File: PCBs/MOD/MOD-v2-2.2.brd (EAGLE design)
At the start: 159.8 x 49.3 mm, 44 parts, among them J1 SERVO1, J10 JOY1, J11 JOY2, J12 RPi-Shutdown, J13 AN5, J14 AN6, J15 AN7, J16 AN8, J17 Battery (Main), J2 SERVO2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

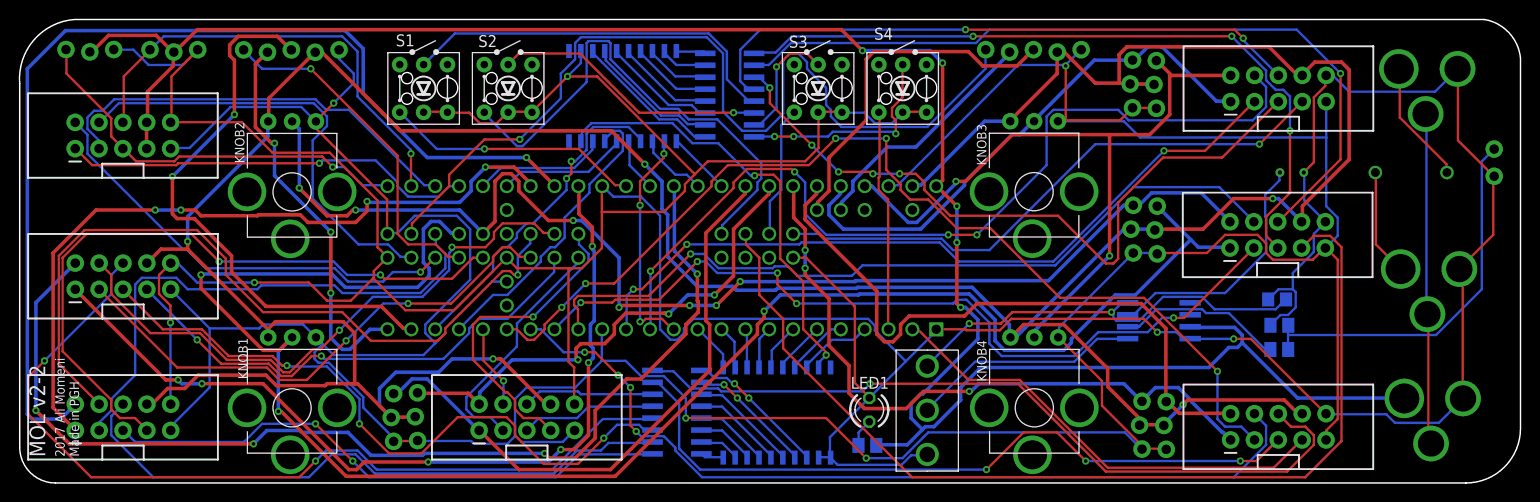
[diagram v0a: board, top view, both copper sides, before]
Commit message: routed teensy breakout for MOD, v2-2.2.brd updated
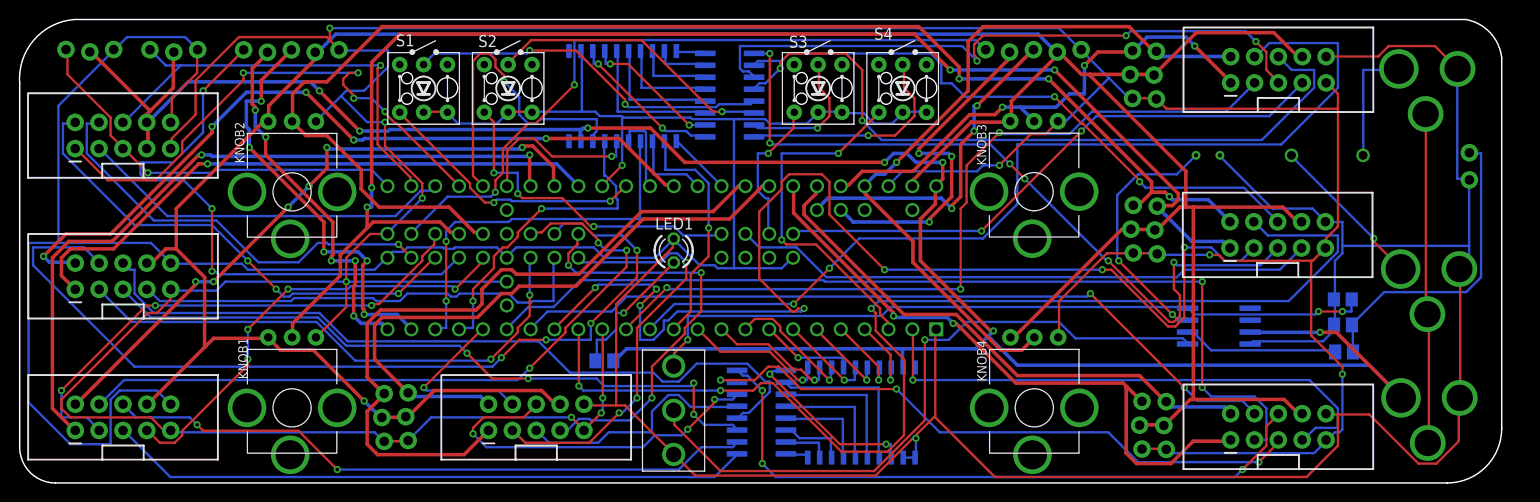
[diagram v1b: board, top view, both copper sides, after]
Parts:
- moved R1 29.4 mm to (62.2, 13.0)
- moved SW2 27.0 mm to (69.6, 7.74)
- moved LED1 26.8 mm to (69.6, 24.7)
- moved RELAY1 9.12 mm to (125.2, 34.9)
- moved RN1 9.00 mm to (79.0, 7.54)
- moved U$1 9.00 mm to (89.6, 7.50)
- moved C1 7.00 mm to (140.9, 19.5)
- moved R2 6.90 mm to (141.0, 13.9)
- moved R3 6.78 mm to (140.9, 16.8)
- moved U1 6.41 mm to (127.7, 16.7)
- moved J12 2.67 mm to (154.3, 35.0)
- moved STRIP6 2.00 mm to (134.0, 44.0)
- moved J13 1.00 mm to (38.7, 4.43)
- moved J14 1.00 mm to (41.2, 4.52)
- moved J8 1.00 mm to (118.3, 40.9)
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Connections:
- removed net V+: U$1.9, U$2.9
- net +5V: now also U$1.9, U$2.9
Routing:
- net V+: track 47.3 -> 0.00 mm, vias 2 -> 0
- net N$3: track 24.5 -> 70.9 mm, vias 0 -> 1
- net AGND: track 369.6 -> 324.3 mm, vias 5 -> 1
- net LED5: track 106.5 -> 62.4 mm
- net AN2: track 110.3 -> 66.9 mm, vias 1 -> 6
- net B10: track 84.3 -> 123.4 mm, vias 1 -> 3
- net B9: track 88.7 -> 124.6 mm, vias 5 -> 7
- net AN9: track 185.8 -> 150.6 mm, vias 3 -> 4
- net B4: track 63.2 -> 96.7 mm, vias 2 -> 4
- net +5V-BATTERY: track 45.3 -> 78.8 mm, vias 2 -> 3
- net +3V3: track 407.4 -> 440.5 mm, vias 4 -> 10
- net AN4: track 114.7 -> 82.7 mm, vias 4 -> 5
- net GND: track 477.7 -> 509.7 mm, vias 5 -> 2
- net AN3: track 91.9 -> 64.1 mm, vias 6 -> 1
- net JOYB2: track 37.0 -> 62.8 mm, vias 1 -> 3
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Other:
- board size 159.8 x 49.3 mm -> 157.8 x 49.3 mm

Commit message: routed teensy breakout for MOD, v2-2.2.brd updated
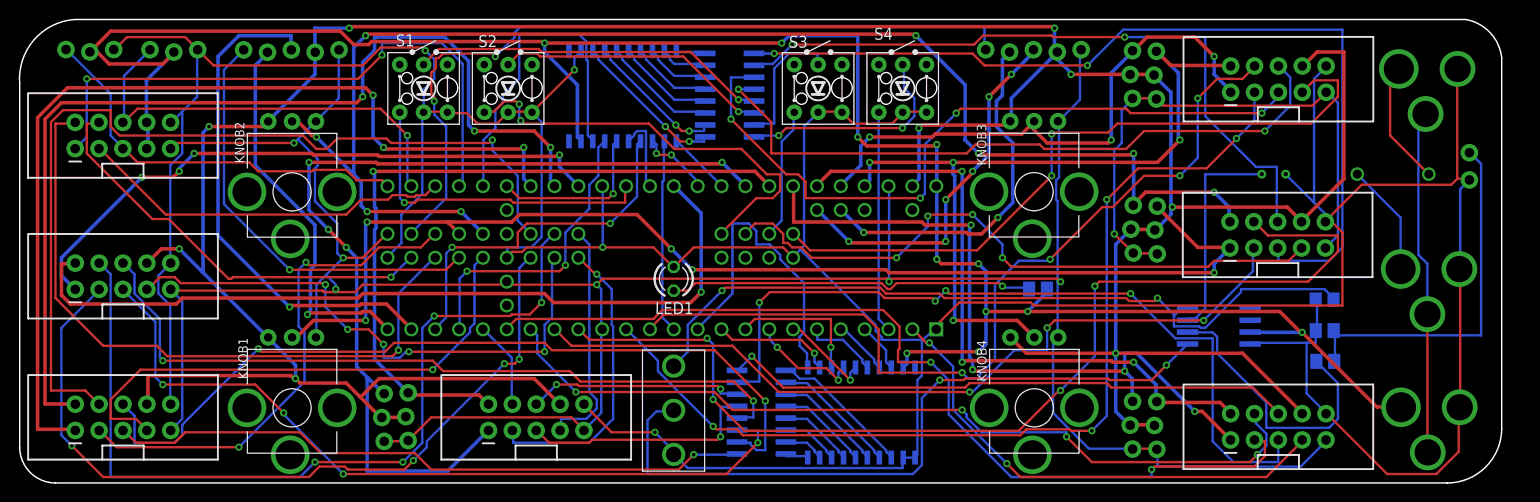
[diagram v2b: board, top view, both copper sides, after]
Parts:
- moved R1 46.8 mm to (108.4, 20.6)
- moved RELAY1 7.28 mm to (132.2, 32.9)
- moved LED1 3.00 mm to (69.6, 21.7)
- moved R2 2.24 mm to (139.0, 12.9)
- moved R3 2.04 mm to (138.9, 16.2)
- moved C1 1.94 mm to (138.9, 19.5)
- moved J15 1.00 mm to (118.3, 3.61)
- moved J16 1.00 mm to (120.9, 3.58)
- moved J17 1.00 mm to (160.7, 8.06)
- moved STRIP6 1.00 mm to (134.0, 43.0)
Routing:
- net +3V3: track 440.5 -> 360.8 mm, vias 10 -> 7
- net GND: track 509.7 -> 456.6 mm, vias 2 -> 4
- net AN2: track 66.9 -> 107.1 mm, vias 6 -> 3
- net B9: track 124.6 -> 86.3 mm, vias 7 -> 3
- net AGND: track 324.3 -> 351.9 mm, vias 1 -> 9
- net B3: track 57.5 -> 84.9 mm, vias 2 -> 4
- net N$2: track 15.0 -> 39.0 mm
- net AN5: track 76.5 -> 100.3 mm, vias 0 -> 4
- net AN9: track 150.6 -> 126.8 mm, vias 4 -> 5
- net AN1: track 78.3 -> 100.1 mm, vias 2 -> 3
- net B2: track 76.3 -> 97.0 mm, vias 3 -> 1
- net LED3: track 45.1 -> 25.0 mm, vias 3 -> 0
- net M_INA: track 52.2 -> 71.6 mm, vias 3 -> 1
- net PWM_2: track 69.5 -> 88.3 mm
- net PWM8: track 15.3 -> 33.7 mm, vias 1 -> 0
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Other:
- board text added: "MOL v2-2.2"
- board text removed: "MOL v2-2"
